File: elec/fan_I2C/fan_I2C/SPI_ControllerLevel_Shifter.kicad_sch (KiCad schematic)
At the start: 33 parts

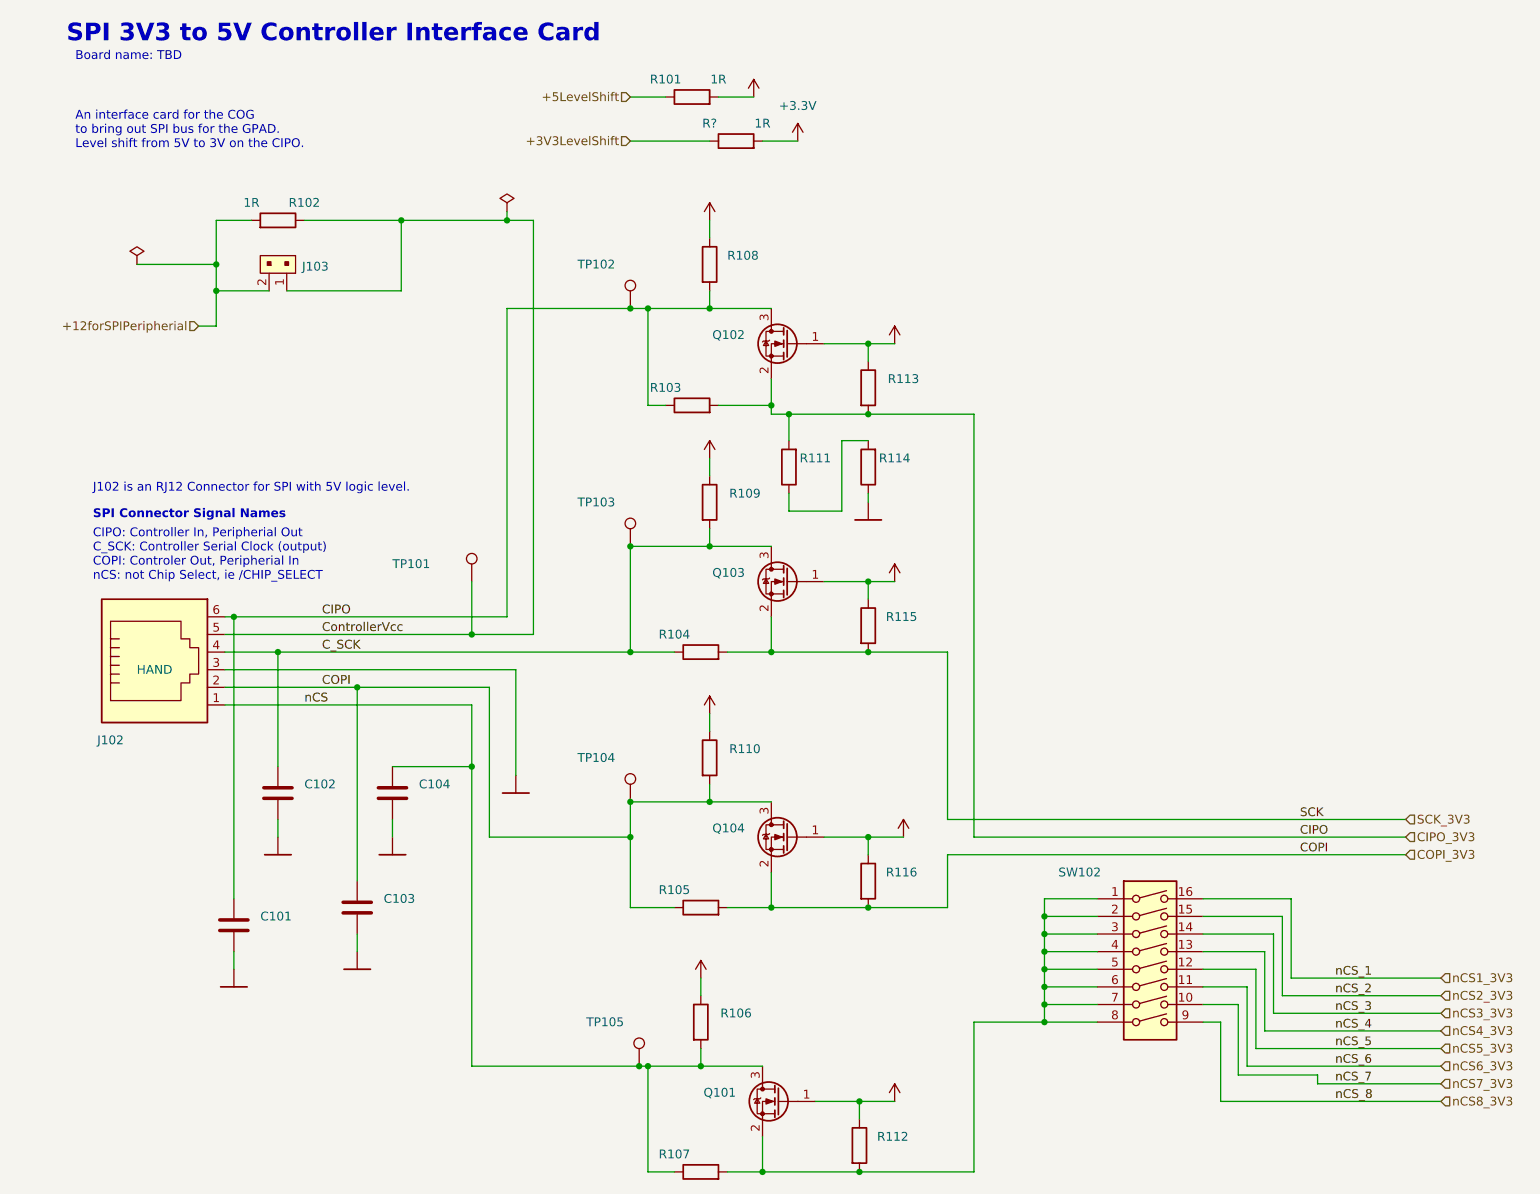
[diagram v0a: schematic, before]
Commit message: Making power local to the sheets.
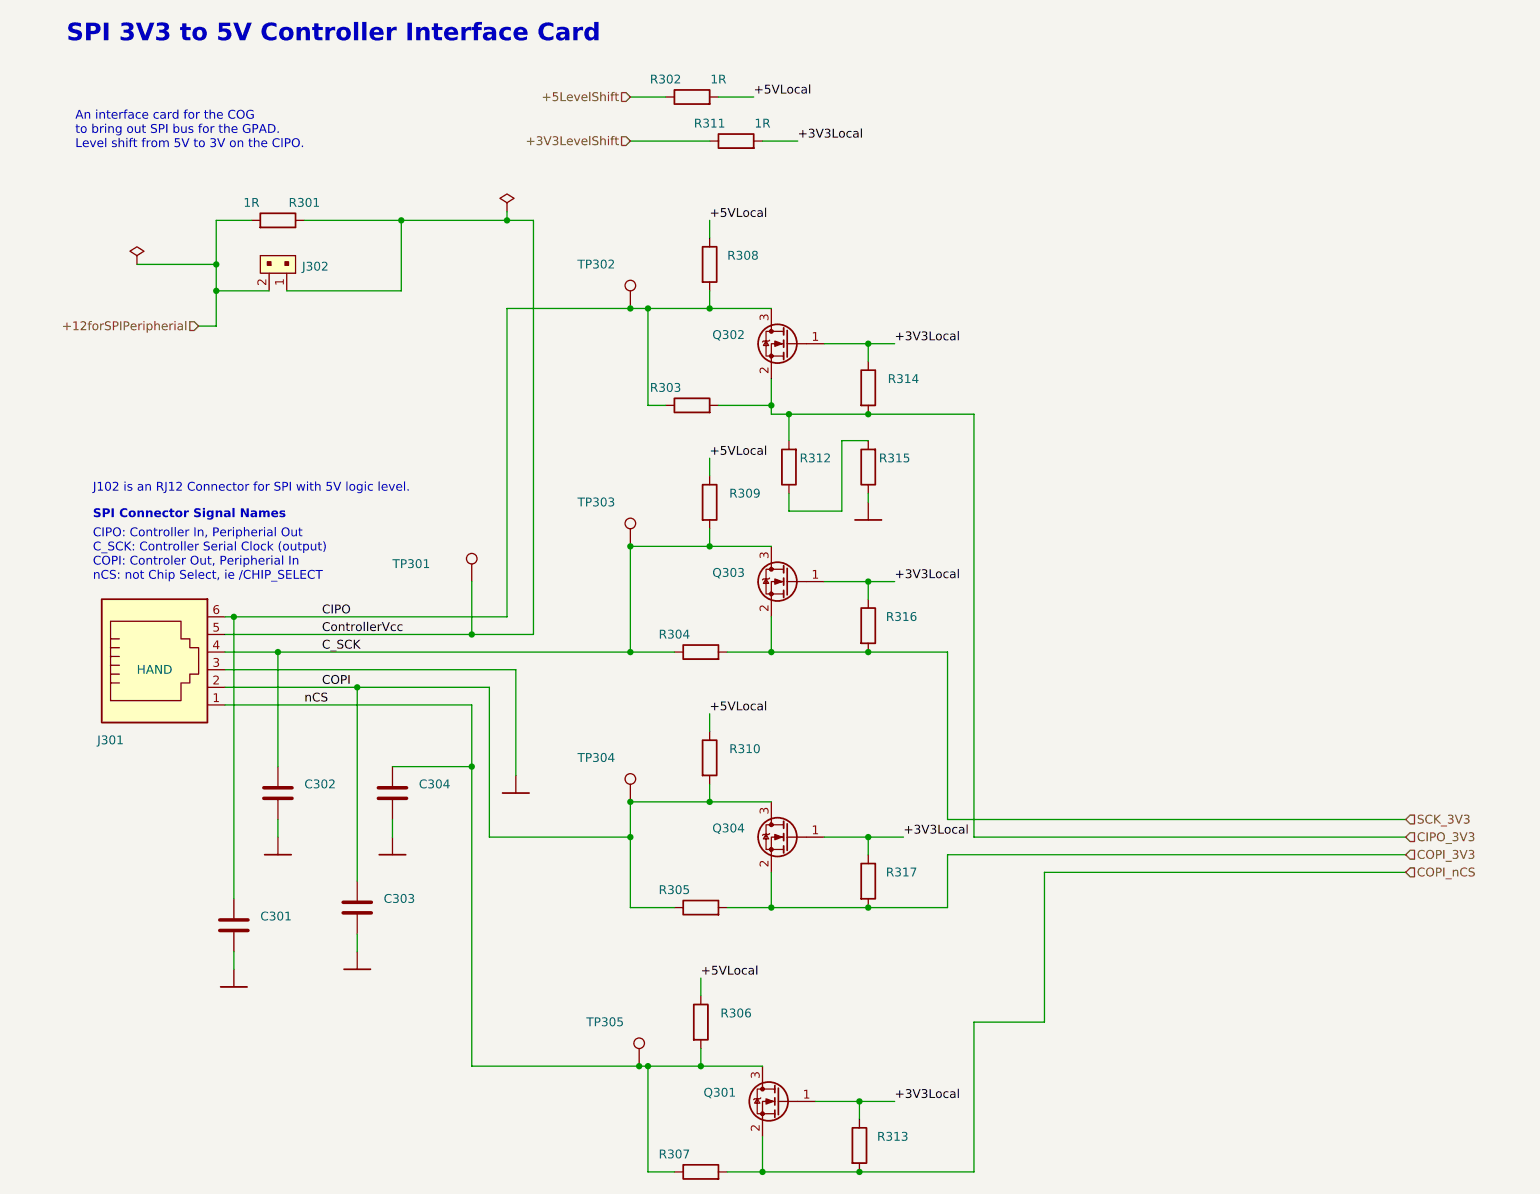
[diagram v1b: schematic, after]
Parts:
- removed SW102: (no value), symbol Switch:SW_DIP_x08
- gave numbers to parts that had none: 1
- renumbered C101 to C301, C102 to C302, C103 to C303, C104 to C304, J102 to J301, J103 to J302, Q101 to Q301, Q102 to Q302, Q103 to Q303, Q104 to Q304, R102 to R301, R101 to R302, R103 to R303, R104 to R304, R105 to R305, R106 to R306, R107 to R307, R108 to R308, R109 to R309, R110 to R310, R111 to R312, R112 to R313, R113 to R314, R114 to R315, R115 to R316, R116 to R317, TP101 to TP301, TP102 to TP302, TP103 to TP303, TP104 to TP304, TP105 to TP305
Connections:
- net CIPO_3V3: no longer C301.1, J301.6, Q302.3 (D), R303.1, R308.2, TP302.1
- net COPI_3V3: no longer C303.1, J301.2, Q304.3 (D), R305.1, R310.2, TP304.1
- net COPI_nCS: now reaches Q301.2 (S), R307.2, R313.2
- net +3.3V renamed +3V3Local
- net +5V renamed +5VLocal
- new net CIPO: C301.1, J301.6, Q302.3 (D), R303.1, R308.2, TP302.1
- new net COPI: C303.1, J301.2, Q304.3 (D), R305.1, R310.2, TP304.1
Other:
- note removed: "Board name: TBD"

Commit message: Add Connectors RJ12 and JST.
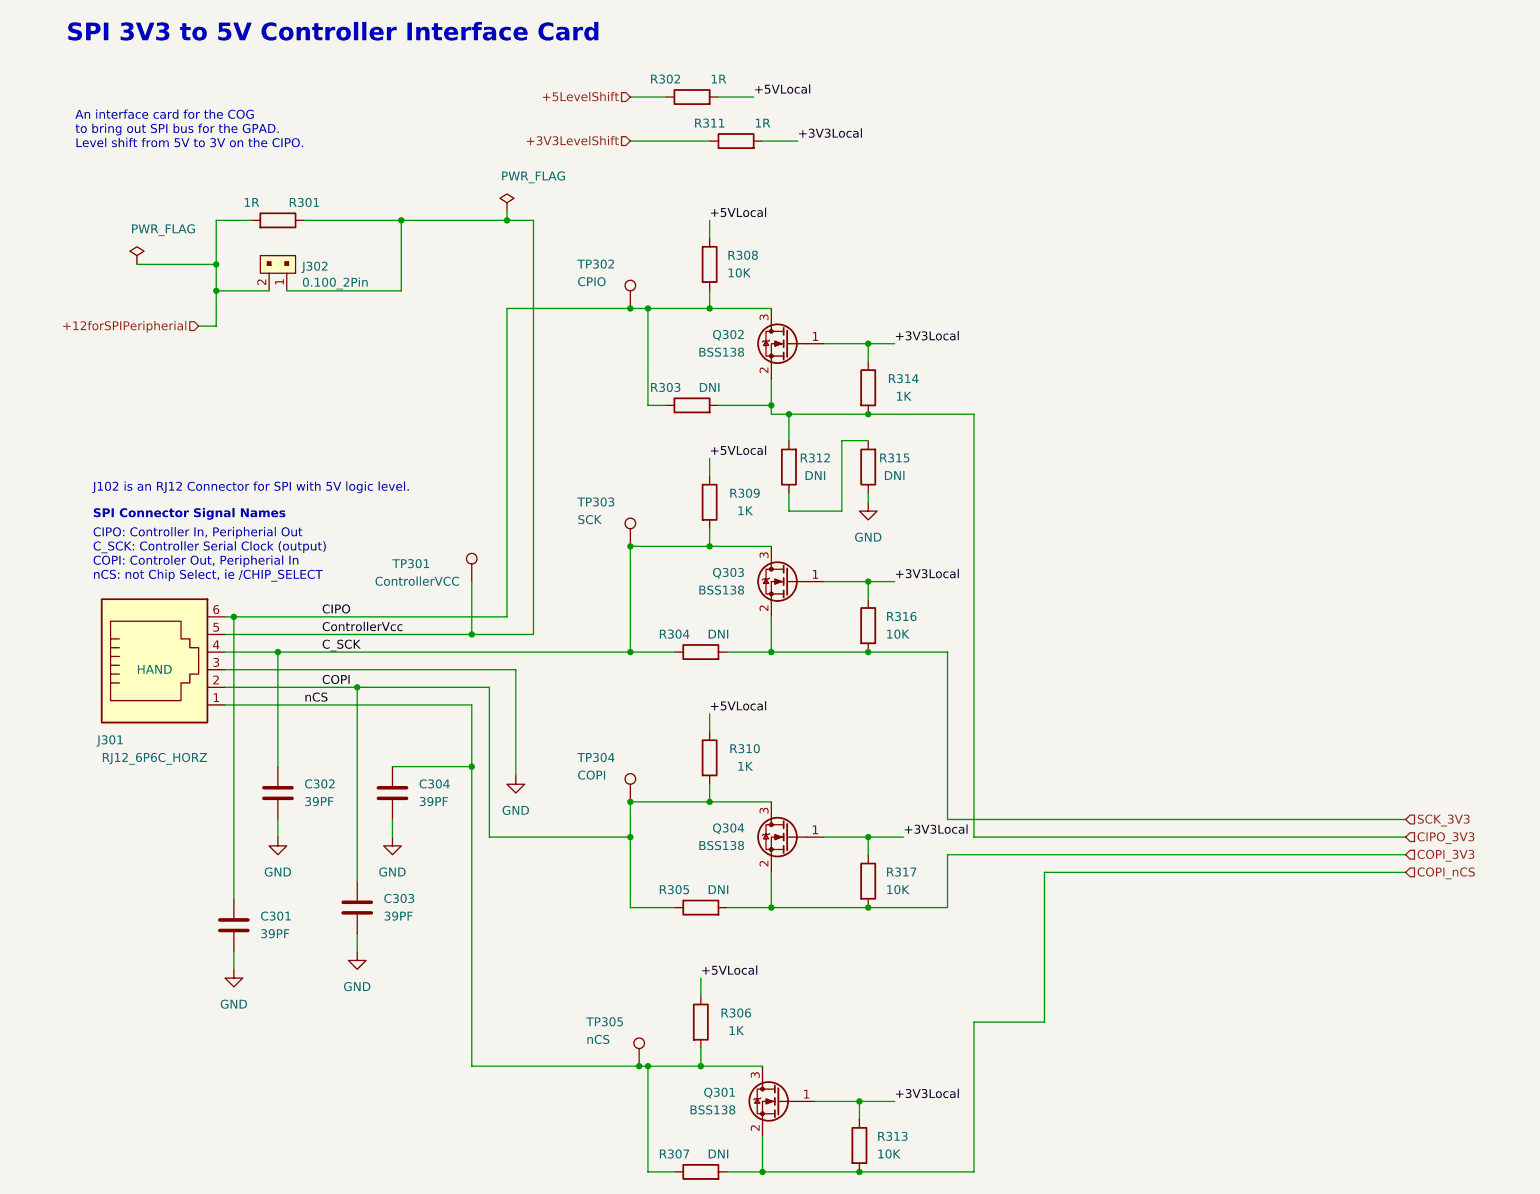
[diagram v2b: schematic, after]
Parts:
- C301, C302, C303, C304: value (none) -> 39PF; footprint (none) -> Capacitor_SMD:C_0603_1608Metric_Pad1.08x0.95mm_HandSolder
- J301: value (none) -> RJ12_6P6C_HORZ; footprint (none) -> PubInv_PCB:RJ12_Amphenol_54601
- J302: value (none) -> 0.100_2Pin; footprint (none) -> Connector_PinHeader_2.54mm:PinHeader_1x02_P2.54mm_Vertical
- Q301, Q302, Q303, Q304: value (none) -> BSS138; footprint (none) -> Package_TO_SOT_SMD:SOT-23
- R303, R304, R305, R307, R312, R315: value (none) -> DNI; footprint (none) -> Resistor_SMD:R_0603_1608Metric_Pad0.98x0.95mm_HandSolder
- R306, R309, R310, R314: value (none) -> 1K; footprint (none) -> Resistor_SMD:R_0603_1608Metric_Pad0.98x0.95mm_HandSolder
- R308, R313, R316, R317: value (none) -> 10K; footprint (none) -> Resistor_SMD:R_0603_1608Metric_Pad0.98x0.95mm_HandSolder
- TP301: value (none) -> ControllerVCC; footprint (none) -> TestPoint:TestPoint_Loop_D2.54mm_Drill1.5mm_Beaded
- TP302: value (none) -> CPIO; footprint (none) -> TestPoint:TestPoint_Loop_D2.54mm_Drill1.5mm_Beaded
- TP303: value (none) -> SCK; footprint (none) -> TestPoint:TestPoint_Loop_D2.54mm_Drill1.5mm_Beaded
- TP304: value (none) -> COPI; footprint (none) -> TestPoint:TestPoint_Loop_D2.54mm_Drill1.5mm_Beaded
- TP305: value (none) -> nCS; footprint (none) -> TestPoint:TestPoint_Loop_D2.54mm_Drill1.5mm_Beaded
